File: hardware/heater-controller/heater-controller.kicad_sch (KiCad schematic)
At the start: 0 parts

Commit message: 回路図，PCB更新
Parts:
- added A1: RaspberryPi_Pico, Module:RaspberryPi_Pico_Common_Unspecified, symbol MCU_Module:RaspberryPi_Pico
- added D101: D_Schottky, Diode_SMD:D_SOD-123, symbol Device:D_Schottky
- added D102: power, LED_SMD:LED_0805_2012Metric, symbol Device:LED
- added J101: pico LiPo, Connector_JST:JST_PH_B2B-PH-K_1x02_P2.00mm_Vertical, symbol Connector_Generic:Conn_01x02
- added R101: 1k, Resistor_SMD:R_0805_2012Metric, symbol Device:R
- added SW101: power, Button_Switch_THT:SW_Slide-03_Wuerth-WS-SLTV_10x2.5x6.4_P2.54mm, symbol Switch:SW_SPST
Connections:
- new net: D101.2 (A), R101.2, SW101.1 (A)
- new net: J101.1 (Pin_1), SW101.2 (B)
- new net: A1.39 (VSYS), D101.1 (K)
- new net: D102.2 (A), R101.1
- new net GND: A1.13 (GND), A1.18 (GND), A1.23 (GND), A1.28 (GND), A1.3 (GND), A1.38 (GND), A1.8 (GND), D102.1 (K), J101.2 (Pin_2)
- new net Heater/bat_heater: A1.31 (GPIO26_ADC0)
- new net Heater/heater_con: A1.21 (GPIO16)
- new net Thermistor/AGND: A1.33 (AGND)
- new net Thermistor/R_Thermistor: A1.32 (GPIO27_ADC1)
- new net VDD: A1.36 (3V3)
- no-connect marks 0 -> 27
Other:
- added sheet Heater (heater.kicad_sch)
- added sheet Thermistor (Thermistor.kicad_sch)

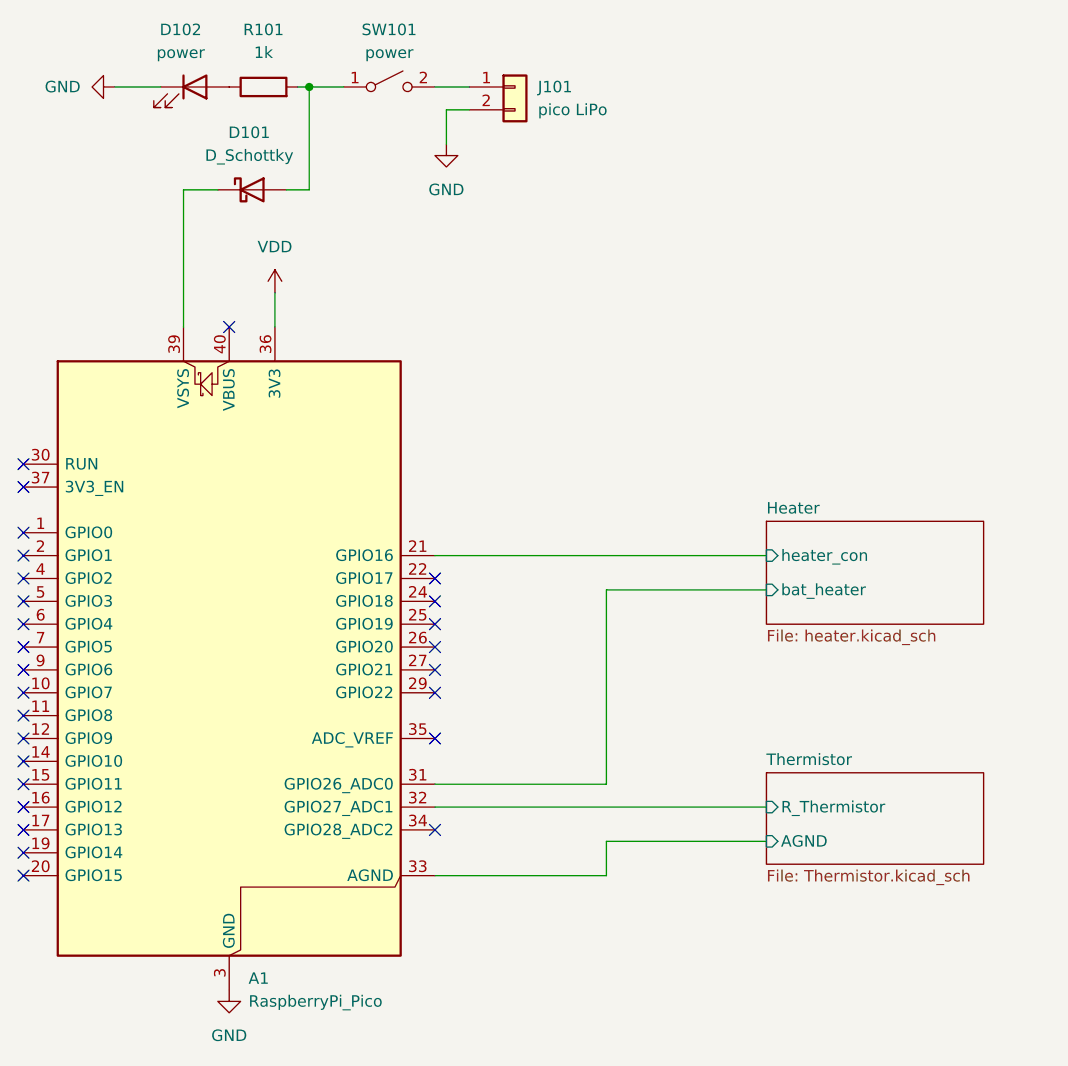
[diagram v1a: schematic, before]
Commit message: BBMで問題がなければ発注可能
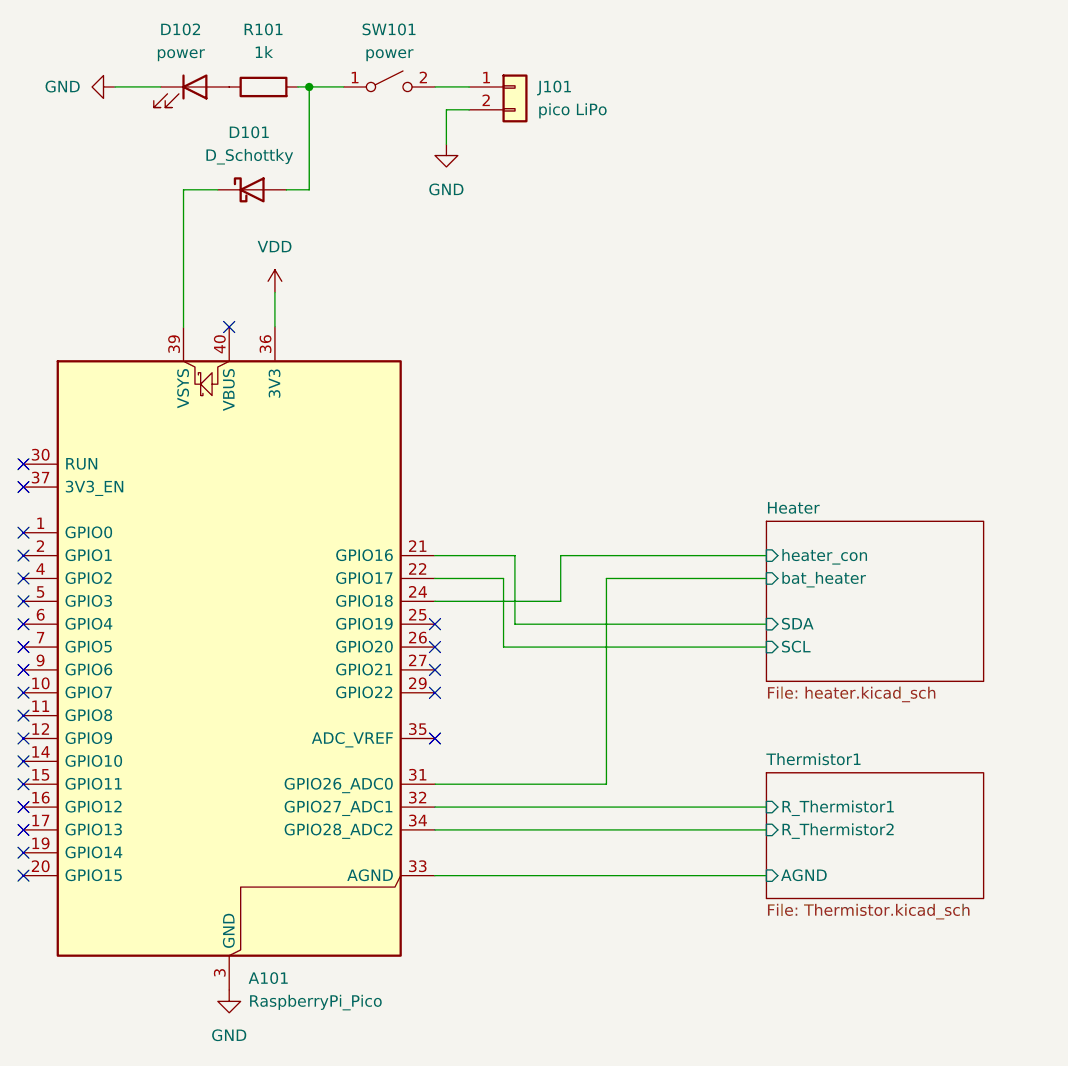
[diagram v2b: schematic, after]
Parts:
- renumbered A1 to A101
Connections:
- net Heater/heater_con: now also A101.24 (GPIO18); no longer A101.21 (GPIO16)
- net Heater/SCL: now reaches A101.22 (GPIO17)
- net Thermistor1/R_Thermistor2: now reaches A101.34 (GPIO28_ADC2)
- net Thermistor1/R_Thermistor renamed Thermistor1/R_Thermistor1
- new net Heater/SDA: A101.21 (GPIO16)
- no-connect marks 27 -> 24
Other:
- sheet Thermistor renamed Thermistor1
- sheet Heater ports: added SCL, SDA; removed none
- sheet Thermistor1 ports: added R_Thermistor1, R_Thermistor2; removed R_Thermistor
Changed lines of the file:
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@@
-	)
-	(no_connect
-		(at 90.17 116.84)
 	)
 	(no_connect
@@
 	)
 	(no_connect
-		(at 90.17 88.9)
-	)
-	(no_connect
 		(at 90.17 106.68)
 	)
@@
 	)
 	(no_connect
-		(at 90.17 91.44)
-	)
-	(no_connect
 		(at 44.45 88.9)
 	)
@@
 	(wire
 		(pts
+			(xy 90.17 116.84) (xy 127 116.84)
+		)
+		(stroke
+			(width 0)
+			(type default)
+		)
+	)
+	(wire
+		(pts
 			(xy 90.17 111.76) (xy 109.22 111.76)
 		)
@@
 	(wire
 		(pts
-			(xy 109.22 90.17) (xy 127 90.17)
+			(xy 109.22 88.9) (xy 127 88.9)
 		)
 		(stroke
@@
 	(wire
 		(pts
+			(xy 90.17 88.9) (xy 97.79 88.9)
+		)
+		(stroke
+			(width 0)
+			(type default)
+		)
+	)
+	(wire
+		(pts
+			(xy 97.79 88.9) (xy 97.79 96.52)
+		)
+		(stroke
+			(width 0)
+			(type default)
+		)
+	)
+	(wire
+		(pts
+			(xy 90.17 91.44) (xy 104.14 91.44)
+		)
+		(stroke
+			(width 0)
+			(type default)
+		)
+	)
+	(wire
+		(pts
+			(xy 99.06 86.36) (xy 99.06 93.98)
+		)
+		(stroke
+			(width 0)
+			(type default)
+		)
+	)
+	(wire
+		(pts
 			(xy 93.98 34.29) (xy 90.17 34.29)
 		)
@@
 	(wire
 		(pts
-			(xy 109.22 111.76) (xy 109.22 90.17)
-		)
-		(stroke
-			(width 0)
-			(type default)
-		)
-	)
-	(wire
-		(pts
-			(xy 127 118.11) (xy 109.22 118.11)
+			(xy 99.06 86.36) (xy 90.17 86.36)
+		)
+		(stroke
+			(width 0)
+			(type default)
+		)
+	)
+	(wire
+		(pts
+			(xy 109.22 111.76) (xy 109.22 88.9)
 		)
 		(stroke
@@
 	(wire
 		(pts
+			(xy 97.79 96.52) (xy 127 96.52)
+		)
+		(stroke
+			(width 0)
+			(type default)
+		)
+	)
+	(wire
+		(pts
 			(xy 74.93 34.29) (xy 76.2 34.29)
 		)
@@
 	(wire
 		(pts
+			(xy 104.14 86.36) (xy 127 86.36)
+		)
+		(stroke
+			(width 0)
+			(type default)
+		)
+	)
+	(wire
+		(pts
 			(xy 76.2 45.72) (xy 73.66 45.72)
 		)
@@
 	(wire
 		(pts
-			(xy 109.22 121.92) (xy 90.17 121.92)
+			(xy 90.17 121.92) (xy 127 121.92)
 		)
 		(stroke
@@
 	(wire
 		(pts
-			(xy 90.17 86.36) (xy 127 86.36)
+			(xy 127 93.98) (xy 99.06 93.98)
 		)
 		(stroke
@@
 	(wire
 		(pts
-			(xy 109.22 118.11) (xy 109.22 121.92)
-		)
-		(stroke
-			(width 0)
-			(type default)
-		)
-	)
-	(wire
-		(pts
 			(xy 66.04 45.72) (xy 62.23 45.72)
 		)
@@
 		(pts
 			(xy 54.61 34.29) (xy 59.69 34.29)
+		)
+		(stroke
+			(width 0)
+			(type default)
+		)
+	)
+	(wire
+		(pts
+			(xy 104.14 91.44) (xy 104.14 86.36)
 		)
 		(stroke
@@
 		(dnp no)
 		(fields_autoplaced yes)
-		(property "Reference" "A1"
+		(property "Reference" "A101"
 			(at 69.4533 133.35 0)
 			(effects
@@
 			(project ""
 				(path "/10d663fd-57cf-4e41-a739-41ba32dcef00"
-					(reference "A1")
+					(reference "A101")
 					(unit 1)
 				)
@@
 	(sheet
 		(at 127 110.49)
-		(size 24.13 10.16)
+		(size 24.13 13.97)
 		(exclude_from_sim no)
 		(in_bom yes)
@@
 			(color 0 0 0 0.0000)
 		)
-		(property "Sheetname" "Thermistor"
+		(property "Sheetname" "Thermistor1"
 			(at 127 109.7784 0)
 			(effects
@@
 		)
 		(property "Sheetfile" "Thermistor.kicad_sch"
-			(at 127 121.2346 0)
+			(at 127 125.0446 0)
 			(effects
 				(font
@@
 			)
 		)
-		(pin "R_Thermistor" input
+		(pin "AGND" input
+			(at 127 121.92 180)
+			(effects
+				(font
+					(size 1.27 1.27)
+				)
+				(justify left)
+			)
+		)
+		(pin "R_Thermistor1" input
 			(at 127 114.3 180)
 			(effects
@@
 			)
 		)
-		(pin "AGND" input
-			(at 127 118.11 180)
+		(pin "R_Thermistor2" input
+			(at 127 116.84 180)
 			(effects
 				(font
@@
 	(sheet
 		(at 127 82.55)
-		(size 24.13 11.43)
+		(size 24.13 17.78)
 		(exclude_from_sim no)
 		(in_bom yes)
@@
 		)
 		(property "Sheetfile" "heater.kicad_sch"
-			(at 127 94.5646 0)
+			(at 127 100.9146 0)
 			(effects
 				(font
@@
 		)
 		(pin "bat_heater" input
-			(at 127 90.17 180)
-			(effects
-				(font
+			(at 127 88.9 180)
+			(effects
+				(font
+					(size 1.27 1.27)
+				)
+				(justify left)
+			)
+		)
+		(pin "SCL" input
+			(at 127 96.52 180)
+			(effects
+				(font
+					(size 1.27 1.27)
+				)
+				(justify left)
+			)
+		)
+		(pin "SDA" input
+			(at 127 93.98 180)
+			(effects
+				(font

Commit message: いろいろ
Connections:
- net Heater/SCL renamed BME280/I2C_SCL
- net Heater/SDA renamed BME280/I2C_SDA
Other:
- added sheet BME280 (Pressure.kicad_sch)
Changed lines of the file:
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@@
 		(color 0 0 0 0)
 	)
+	(junction
+		(at 99.06 86.36)
+		(diameter 0)
+		(color 0 0 0 0)
+	)
+	(junction
+		(at 97.79 88.9)
+		(diameter 0)
+		(color 0 0 0 0)
+	)
 	(no_connect
 		(at 90.17 93.98)
@@
 	(wire
 		(pts
+			(xy 97.79 66.04) (xy 97.79 88.9)
+		)
+		(stroke
+			(width 0)
+			(type default)
+		)
+	)
+	(wire
+		(pts
 			(xy 109.22 88.9) (xy 127 88.9)
 		)
@@
 	(wire
 		(pts
+			(xy 127 71.12) (xy 99.06 71.12)
+		)
+		(stroke
+			(width 0)
+			(type default)
+		)
+	)
+	(wire
+		(pts
+			(xy 99.06 71.12) (xy 99.06 86.36)
+		)
+		(stroke
+			(width 0)
+			(type default)
+		)
+	)
+	(wire
+		(pts
 			(xy 109.22 111.76) (xy 109.22 88.9)
+		)
+		(stroke
+			(width 0)
+			(type default)
+		)
+	)
+	(wire
+		(pts
+			(xy 97.79 66.04) (xy 127 66.04)
 		)
 		(stroke
@@
 				)
 			)
+		)
+	)
+	(sheet
+		(at 127 60.96)
+		(size 24.13 15.24)
+		(exclude_from_sim no)
+		(in_bom yes)
+		(on_board yes)
+		(dnp no)
+		(fields_autoplaced yes)
+		(stroke
+			(width 0.1524)
+			(type solid)
+		)
+		(fill
+			(color 0 0 0 0.0000)
+		)
+		(property "Sheetname" "BME280"
+			(at 127 60.2484 0)
+			(effects
+				(font
+					(size 1.27 1.27)
+				)
+				(justify left bottom)
+			)
+		)
+		(property "Sheetfile" "Pressure.kicad_sch"
+			(at 127 76.7846 0)
+			(effects
+				(font
+					(size 1.27 1.27)
+				)
+				(justify left top)
+			)
+		)
+		(pin "I2C_SCL" bidirectional
+			(at 127 66.04 180)
+			(effects
+				(font
+					(size 1.27 1.27)
+				)
+				(justify left)
+			)
+		)
+		(pin "I2C_SDA" bidirectional
+			(at 127 71.12 180)
+			(effects
+				(font
+					(size 1.27 1.27)
+				)
+				(justify left)
+			)
+		)
+		(instances
+			(project "heater-controller"
+				(path "/10d663fd-57cf-4e41-a739-41ba32dcef00"
+					(page "4")
+				)
+			)
